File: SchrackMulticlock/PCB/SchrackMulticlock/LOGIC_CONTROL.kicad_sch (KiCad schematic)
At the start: 7 parts, among them U2 LDD080AUE-101A, U3 LDD080AUE-101A, U4 LDD080AUE-101A, U5 MAX7219

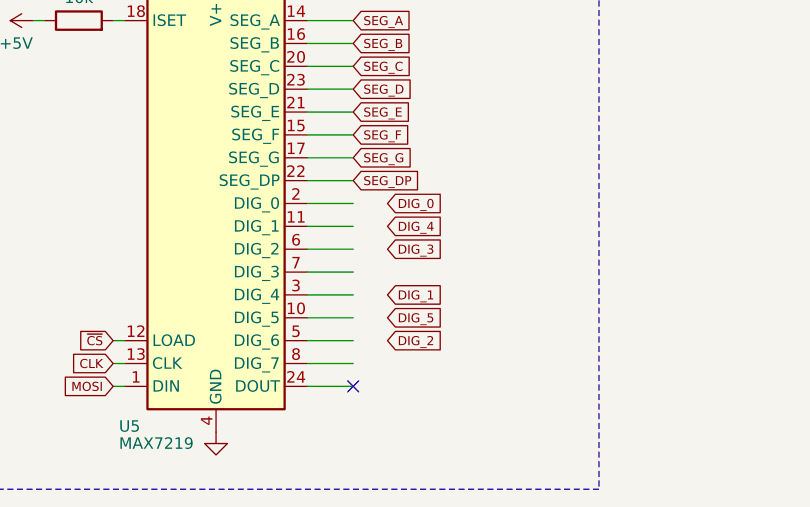
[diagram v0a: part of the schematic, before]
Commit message: Multiclock a lot of routing and layout
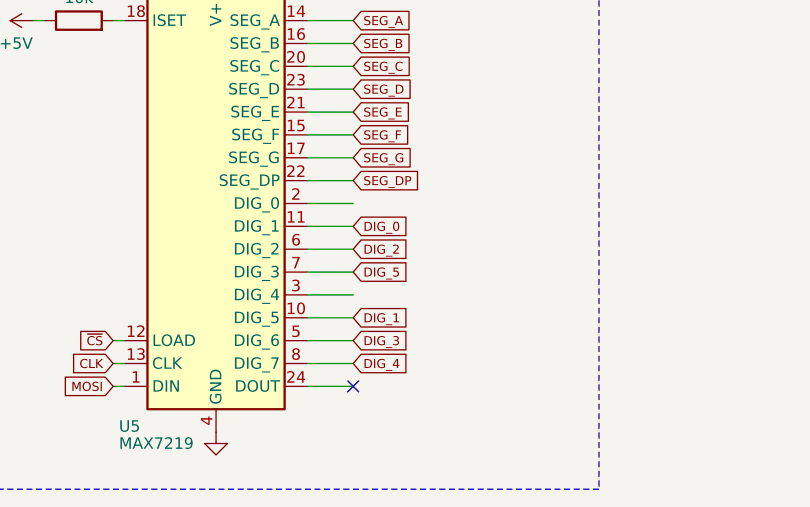
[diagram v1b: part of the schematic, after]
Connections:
- net DIG_0: now also U5.11 (DIG_1)
- net DIG_1: now also U5.10 (DIG_5)
- net DIG_2: now also U5.6 (DIG_2)
- net DIG_3: now also U5.5 (DIG_6)
- net DIG_4: now also U5.8 (DIG_7)
- net DIG_5: now also U5.7 (DIG_3)
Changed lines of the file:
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@@
 	(global_label "DIG_4"
 		(shape input)
-		(at 219.71 97.79 0)
-		(fields_autoplaced yes)
-		(effects
-			(font
-				(face "Bahnschrift")
-				(size 1 1)
-				(color 0 0 0 1)
-			)
-			(justify left)
-		)
-		(property "Intersheetrefs" "${INTERSHEET_REFS}"
-			(at 225.4854 97.79 0)
+		(at 215.9 113.03 0)
+		(fields_autoplaced yes)
+		(effects
+			(font
+				(face "Bahnschrift")
+				(size 1 1)
+				(color 0 0 0 1)
+			)
+			(justify left)
+		)
+		(property "Intersheetrefs" "${INTERSHEET_REFS}"
+			(at 221.6754 113.03 0)
 			(effects
 				(font
@@
 		)
 	)
+	(global_label "DIG_2"
+		(shape input)
+		(at 215.9 100.33 0)
+		(fields_autoplaced yes)
+		(effects
+			(font
+				(face "Bahnschrift")
+				(size 1 1)
+				(color 0 0 0 1)
+			)
+			(justify left)
+		)
+		(property "Intersheetrefs" "${INTERSHEET_REFS}"
+			(at 221.6021 100.33 0)
+			(effects
+				(font
+					(size 1.27 1.27)
+				)
+				(justify left)
+				(hide yes)
+			)
+		)
+	)
 	(global_label "SEG_DP"
 		(shape input)
@@
 		)
 	)
-	(global_label "DIG_2"
-		(shape input)
-		(at 219.71 110.49 0)
-		(fields_autoplaced yes)
-		(effects
-			(font
-				(face "Bahnschrift")
-				(size 1 1)
-				(color 0 0 0 1)
-			)
-			(justify left)
-		)
-		(property "Intersheetrefs" "${INTERSHEET_REFS}"
-			(at 225.4121 110.49 0)
-			(effects
-				(font
-					(size 1.27 1.27)
-				)
-				(justify left)
-				(hide yes)
-			)
-		)
-	)
 	(global_label "SEG_C"
 		(shape input)
@@
 	(global_label "DIG_5"
 		(shape input)
-		(at 219.71 107.95 0)
-		(fields_autoplaced yes)
-		(effects
-			(font
-				(face "Bahnschrift")
-				(size 1 1)
-				(color 0 0 0 1)
-			)
-			(justify left)
-		)
-		(property "Intersheetrefs" "${INTERSHEET_REFS}"
-			(at 225.4512 107.95 0)
+		(at 215.9 102.87 0)
+		(fields_autoplaced yes)
+		(effects
+			(font
+				(face "Bahnschrift")
+				(size 1 1)
+				(color 0 0 0 1)
+			)
+			(justify left)
+		)
+		(property "Intersheetrefs" "${INTERSHEET_REFS}"
+			(at 221.6412 102.87 0)
 			(effects
 				(font
@@
 	(global_label "DIG_1"
 		(shape input)
-		(at 219.71 105.41 0)
-		(fields_autoplaced yes)
-		(effects
-			(font
-				(face "Bahnschrift")
-				(size 1 1)
-				(color 0 0 0 1)
-			)
-			(justify left)
-		)
-		(property "Intersheetrefs" "${INTERSHEET_REFS}"
-			(at 225.1542 105.41 0)
+		(at 215.9 107.95 0)
+		(fields_autoplaced yes)
+		(effects
+			(font
+				(face "Bahnschrift")
+				(size 1 1)
+				(color 0 0 0 1)
+			)
+			(justify left)
+		)
+		(property "Intersheetrefs" "${INTERSHEET_REFS}"
+			(at 221.3442 107.95 0)
 			(effects
 				(font
@@
 	(global_label "DIG_0"
 		(shape input)
-		(at 219.71 95.25 0)
-		(fields_autoplaced yes)
-		(effects
-			(font
-				(face "Bahnschrift")
-				(size 1 1)
-				(color 0 0 0 1)
-			)
-			(justify left)
-		)
-		(property "Intersheetrefs" "${INTERSHEET_REFS}"
-			(at 225.461 95.25 0)
+		(at 215.9 97.79 0)
+		(fields_autoplaced yes)
+		(effects
+			(font
+				(face "Bahnschrift")
+				(size 1 1)
+				(color 0 0 0 1)
+			)
+			(justify left)
+		)
+		(property "Intersheetrefs" "${INTERSHEET_REFS}"
+			(at 221.651 97.79 0)
 			(effects
 				(font
@@
 	(global_label "DIG_3"
 		(shape input)
-		(at 219.71 100.33 0)
-		(fields_autoplaced yes)
-		(effects
-			(font
-				(face "Bahnschrift")
-				(size 1 1)
-				(color 0 0 0 1)
-			)
-			(justify left)
-		)
-		(property "Intersheetrefs" "${INTERSHEET_REFS}"
-			(at 225.4287 100.33 0)
-			(effects
-				(font
+		(at 215.9 110.49 0)
+		(fields_autoplaced yes)
+		(effects
+			(font
+				(face "Bahnschrift")
+				(size 1 1)
+				(color 0 0 0 1)
+			)
+			(justify left)
+		)
+		(property "Intersheetrefs" "${INTERSHEET_REFS}"
+			(at 221.6187 110.49 0)
+			(effects
+				(font

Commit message: PCB order plotting
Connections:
- no-connect marks 1 -> 3
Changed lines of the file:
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@@
+	)
+	(no_connect
+		(at 215.9 105.41)
 	)
 	(no_connect
 		(at 215.9 115.57)
 	)
+	(no_connect
+		(at 215.9 95.25)
+	)
 	(wire
